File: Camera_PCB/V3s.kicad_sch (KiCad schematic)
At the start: 1 part, among them U2 V3s-eLQFP128

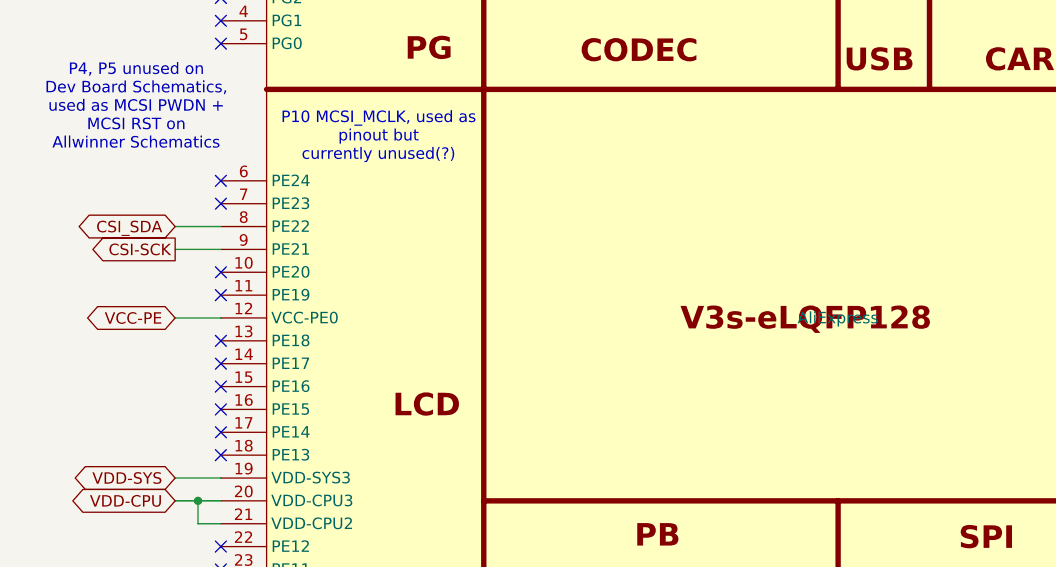
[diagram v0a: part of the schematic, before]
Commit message: Thorough Camera PCB Review by Jack
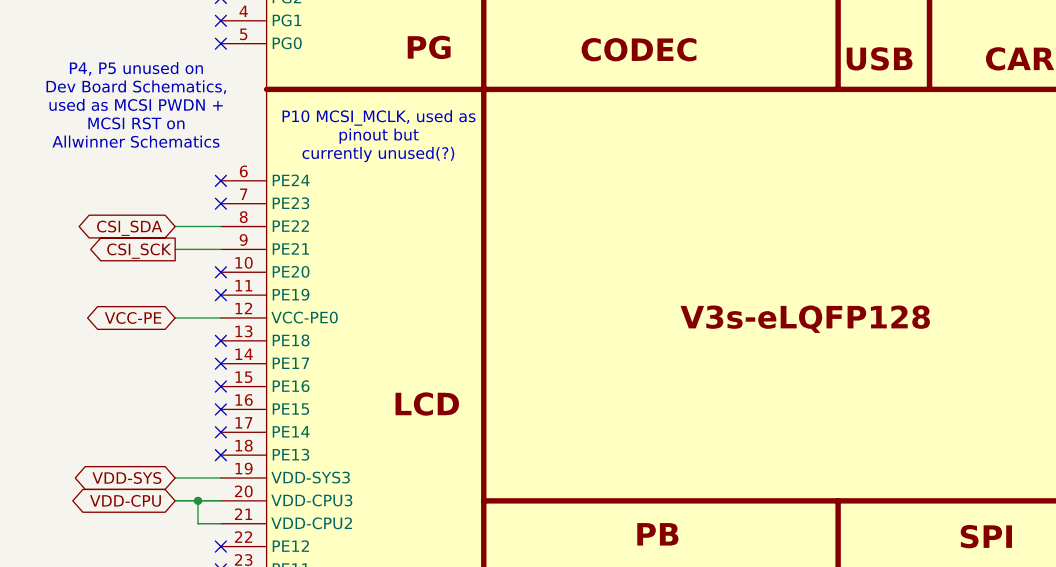
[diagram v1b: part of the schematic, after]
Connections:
- net CSI-SCK renamed CSI_SCK
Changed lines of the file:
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@@
 		)
 	)
-	(global_label "CSI-SCK"
+	(global_label "CSI_SCK"
 		(shape output)
 		(at 34.29 95.25 180)
@@
 		)
 		(property "Intersheetrefs" "${INTERSHEET_REFS}"
-			(at 22.8986 95.25 0)
+			(at 23.5034 95.25 0)
 			(effects
 				(font
@@
 			)
 		)
-		(property "Description" ""
+		(property "Description" "Allwinner V3S ARM CortexTM-A7 CPU 1.2GHz DVR/IPC SOC w/ integrated 64Mbit RAM"
 			(at 107.95 102.87 0)
 			(effects
@@
 					(size 1.27 1.27)
 				)
+				(hide yes)
 			)
 		)
@@
 					(size 1.27 1.27)
 				)
-			)
-		)
+				(hide yes)
+			)
+		)

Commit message: more schematic changes, added solder bridges, etc
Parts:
- added H1, H2, H3, H4: MountingHole, MountingHole:MountingHole_2.2mm_M2, symbol Mechanical:MountingHole

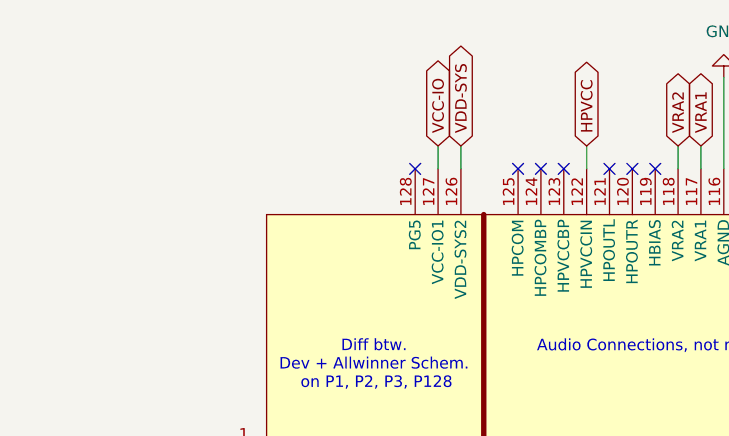
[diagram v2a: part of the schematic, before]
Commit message: PCB has no missing connections, (some missing grounds)
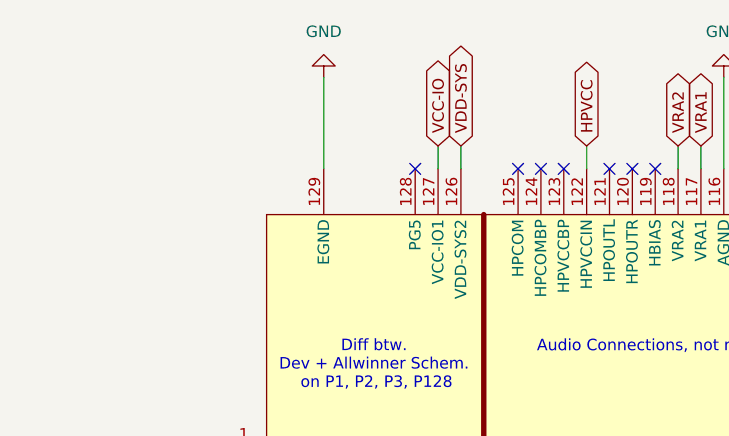
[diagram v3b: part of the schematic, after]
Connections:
- net GND: now also U2.129 (EGND)
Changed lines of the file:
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@@
+	(wire
+		(pts
+			(xy 50.8 21.59) (xy 50.8 31.75)
+		)
+		(stroke
+			(width 0)
+			(type default)
+		)
+	)
 	(wire
 		(pts
@@
 	)
 	(symbol
+		(lib_id "power:GND")
+		(at 50.8 21.59 180)
+		(unit 1)
+		(exclude_from_sim no)
+		(in_bom yes)
+		(on_board yes)
+		(dnp no)
+		(fields_autoplaced yes)
+		(property "Reference" "#PWR044"
+			(at 50.8 15.24 0)
+			(effects
+				(font
+					(size 1.27 1.27)
+				)
+				(hide yes)
+			)
+		)
+		(property "Value" "GND"
+			(at 50.8 16.51 0)
+			(effects
+				(font
+					(size 1.27 1.27)
+				)
+			)
+		)
+		(property "Footprint" ""
+			(at 50.8 21.59 0)
+			(effects
+				(font
+					(size 1.27 1.27)
+				)
+				(hide yes)
+			)
+		)
+		(property "Datasheet" ""
+			(at 50.8 21.59 0)
+			(effects
+				(font
+					(size 1.27 1.27)
+				)
+				(hide yes)
+			)
+		)
+		(property "Description" "Power symbol creates a global label with name \"GND\" , ground"
+			(at 50.8 21.59 0)
+			(effects
+				(font
+					(size 1.27 1.27)
+				)
+				(hide yes)
+			)
+		)
+		(pin "1"
+		)
+		(instances
+			(project "CameraPCB"
+				(path "/400c1603-202c-4359-a830-d2f0d06dd3ce/47962aac-64be-4928-9c9c-c3ab3aab91c0"
+					(reference "#PWR044")
+					(unit 1)
+				)
+			)
+		)
+	)
+	(symbol
 		(lib_id "Mechanical:MountingHole")
 		(at 226.06 110.49 0)
@@
 		(pin "35"
 		)
+		(pin "129"
+		)
 		(instances
